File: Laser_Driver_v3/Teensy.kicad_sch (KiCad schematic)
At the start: 2 parts, among them U37 CR2013-MI2120

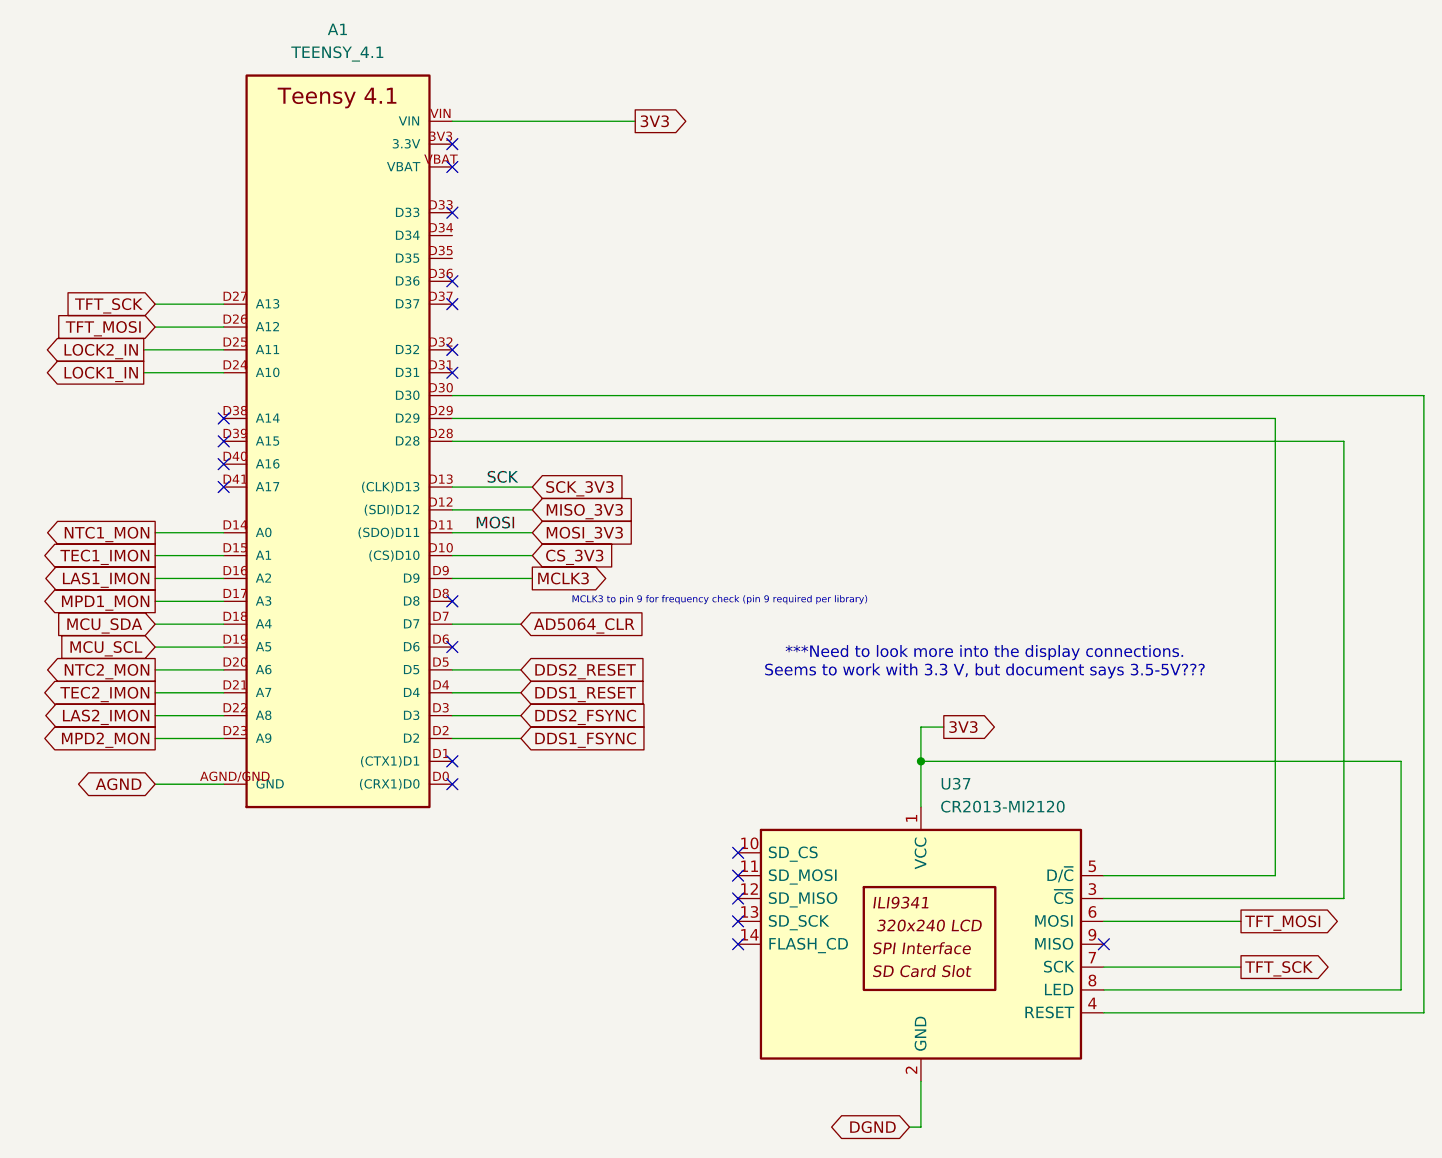
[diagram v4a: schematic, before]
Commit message: Many changes.  Working through ERC.
Main changes are for the grounds.  I found the NETTIE function to tie the GND, DGND and AGND together at a specific point on the boud with a footprint even.
Changed transformers one more time to be consistent for both.
Updated footprints to be consistent and avoid power input/output errors with the ERC.
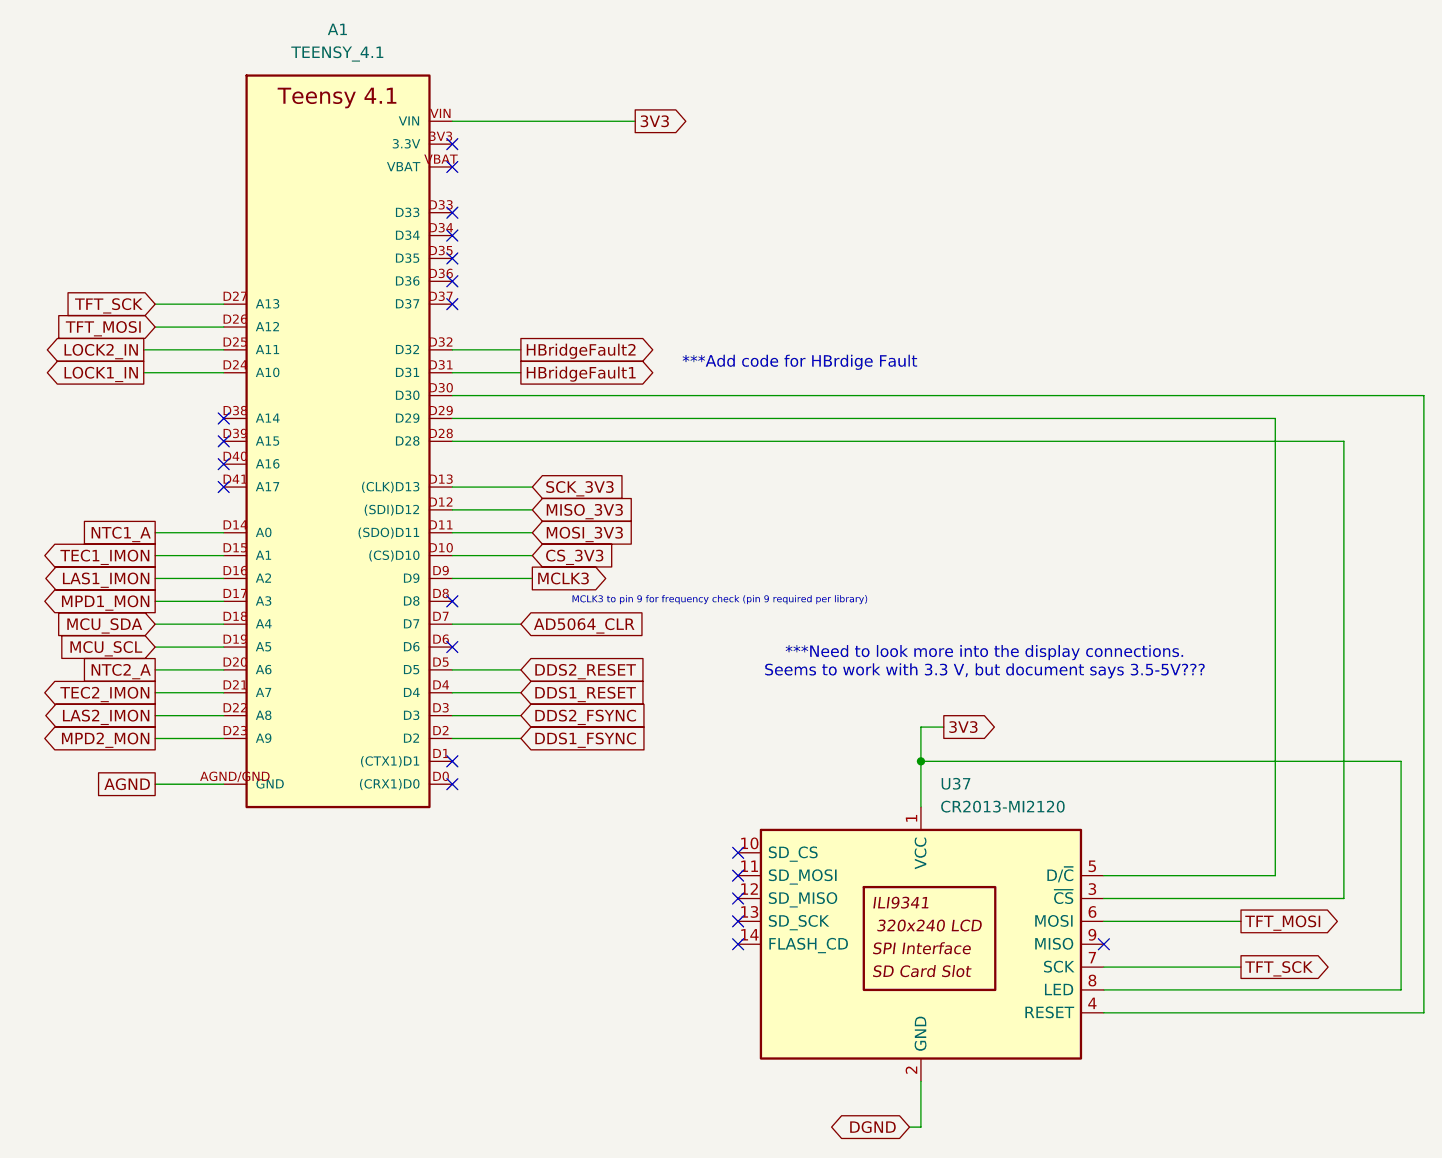
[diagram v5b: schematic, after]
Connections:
- net HBridgeFault1: now reaches A1.D31
- net HBridgeFault2: now reaches A1.D32
- net NTC1_MON renamed NTC1_A
- net NTC2_MON renamed NTC2_A
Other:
- note added: "***Add code for HBrdige Fault"
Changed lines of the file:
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@@
 	(generator_version "10.0")
 	(paper "A4")
+	(text "***Add code for HBrdige Fault"
+		(exclude_from_sim no)
+		(at 116.078 61.214 0)
+		(effects
+			(font
+				(size 1.27 1.27)
+			)
+		)
+	)
 	(text "***Need to look more into the display connections.\nSeems to work with 3.3 V, but document says 3.5-5V???\n"
 		(exclude_from_sim no)
@@
 	)
 	(no_connect
-		(at 77.47 62.23)
-	)
-	(no_connect
 		(at 77.47 92.71)
 	)
@@
 	)
 	(no_connect
-		(at 77.47 59.69)
-	)
-	(no_connect
 		(at 77.47 105.41)
 	)
@@
 	)
 	(no_connect
+		(at 77.47 46.99)
+	)
+	(no_connect
 		(at 149.86 125.73)
 	)
 	(no_connect
+		(at 77.47 49.53)
+	)
+	(no_connect
 		(at 52.07 74.93)
 	)
@@
 	(wire
 		(pts
+			(xy 77.47 62.23) (xy 85.09 62.23)
+		)
+		(stroke
+			(width 0)
+			(type default)
+		)
+	)
+	(wire
+		(pts
 			(xy 44.45 107.95) (xy 52.07 107.95)
 		)
@@
 	(wire
 		(pts
+			(xy 77.47 59.69) (xy 85.09 59.69)
+		)
+		(stroke
+			(width 0)
+			(type default)
+		)
+	)
+	(wire
+		(pts
 			(xy 77.47 97.79) (xy 85.09 97.79)
 		)
@@
 		)
 	)
-	(label "SCK"
-		(at 81.28 74.93 0)
-		(effects
-			(font
-				(size 1.27 1.27)
-			)
-			(justify left bottom)
-		)
-	)
-	(label "MOSI"
-		(at 80.01 80.01 0)
-		(effects
-			(font
-				(size 1.27 1.27)
-			)
-			(justify left bottom)
-		)
-	)
 	(global_label "CS_3V3"
 		(shape input)
@@
 		)
 	)
+	(global_label "HBridgeFault2"
+		(shape output)
+		(at 85.09 59.69 0)
+		(fields_autoplaced yes)
+		(effects
+			(font
+				(size 1.27 1.27)
+			)
+			(justify left)
+		)
+		(property "Intersheetrefs" "${INTERSHEET_REFS}"
+			(at 101.4403 59.69 0)
+			(hide yes)
+			(show_name no)
+			(do_not_autoplace no)
+			(effects
+				(font
+					(size 1.27 1.27)
+				)
+				(justify left)
+			)
+		)
+	)
 	(global_label "MOSI_3V3"
 		(shape input)
@@
 		)
 	)
+	(global_label "HBridgeFault1"
+		(shape output)
+		(at 85.09 62.23 0)
+		(fields_autoplaced yes)
+		(effects
+			(font
+				(size 1.27 1.27)
+			)
+			(justify left)
+		)
+		(property "Intersheetrefs" "${INTERSHEET_REFS}"
+			(at 101.4403 62.23 0)
+			(hide yes)
+			(show_name no)
+			(do_not_autoplace no)
+			(effects
+				(font
+					(size 1.27 1.27)
+				)
+				(justify left)
+			)
+		)
+	)
 	(global_label "TFT_MOSI"
 		(shape output)
@@
 		)
 	)
-	(global_label "NTC1_MON"
-		(shape output)
+	(global_label "NTC1_A"
+		(shape passive)
 		(at 44.45 80.01 180)
 		(fields_autoplaced yes)
@@
 		)
 		(property "Intersheetrefs" "${INTERSHEET_REFS}"
-			(at 31.6072 80.01 0)
+			(at 35.7423 80.01 0)
 			(hide yes)
 			(show_name no)
@@
 	)
 	(global_label "AGND"
-		(shape bidirectional)
+		(shape passive)
 		(at 44.45 107.95 180)
 		(fields_autoplaced yes)
@@
 		)
 		(property "Intersheetrefs" "${INTERSHEET_REFS}"
-			(at 35.3944 107.95 0)
+			(at 37.617 107.95 0)
 			(hide yes)
 			(show_name no)
@@
 		)
 	)
-	(global_label "NTC2_MON"
-		(shape output)
+	(global_label "NTC2_A"
+		(shape passive)
 		(at 44.45 95.25 180)
 		(fields_autoplaced yes)
@@
 		)
 		(property "Intersheetrefs" "${INTERSHEET_REFS}"
-			(at 31.6072 95.25 0)
+			(at 35.7423 95.25 0)
 			(hide yes)
 			(show_name no)

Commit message: Added software limit to TEC current, Hbridge Fault
Software limit to TEC current.  Monitors up to 2.5 A, then flags and reduces setting.
Hbridge fault now wired to Teensy and software flags.
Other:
- note removed: "***Add code for HBrdige Fault"
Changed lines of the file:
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@@
 	(generator_version "10.0")
 	(paper "A4")
-	(text "***Add code for HBrdige Fault"
-		(exclude_from_sim no)
-		(at 116.078 61.214 0)
-		(effects
-			(font
-				(size 1.27 1.27)
-			)
-		)
-	)
 	(text "***Need to look more into the display connections.\nSeems to work with 3.3 V, but document says 3.5-5V???\n"
 		(exclude_from_sim no)

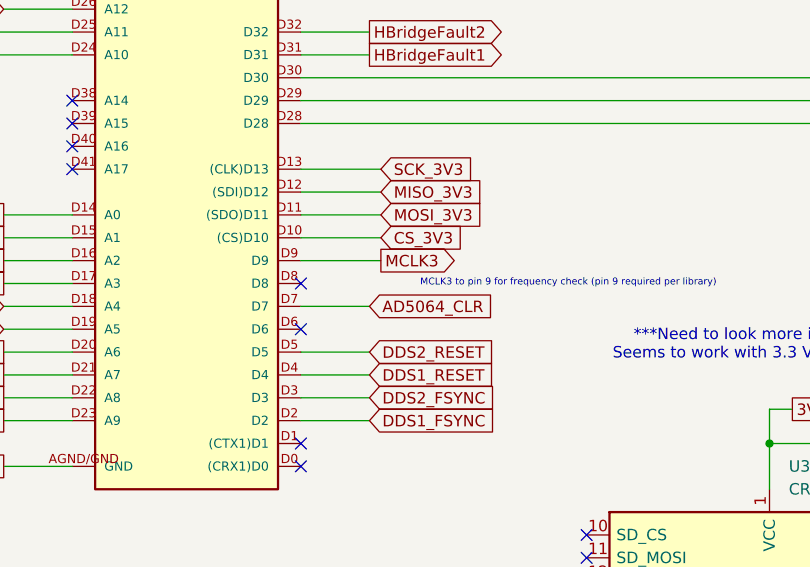
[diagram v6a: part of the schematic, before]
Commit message: 6 V supply. Annotations. Teensy zero current.
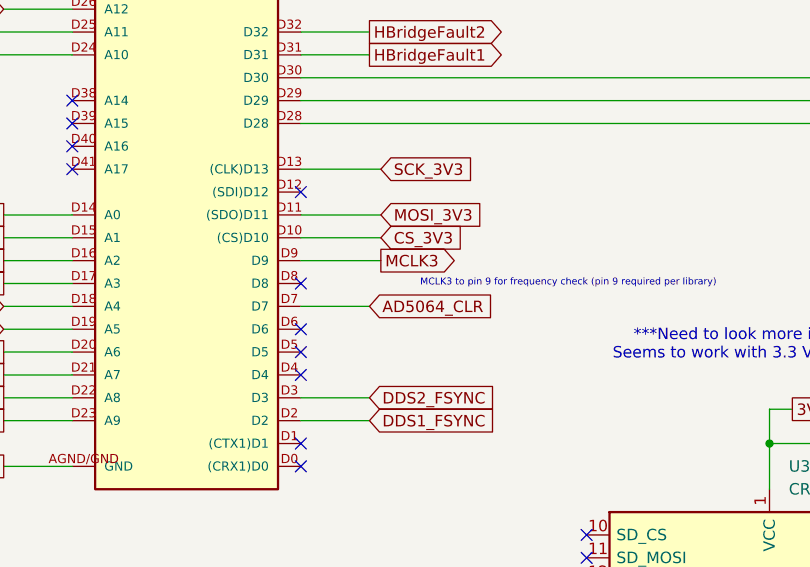
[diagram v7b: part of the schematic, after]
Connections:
- net DDS1_RESET: no longer names the net of A1.D4
- net DDS2_RESET: no longer names the net of A1.D5
- net MISO_3V3: no longer names the net of A1.D12 ((SDI)D12)
- no-connect marks 21 -> 24
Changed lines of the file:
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@@
 	)
 	(no_connect
+		(at 77.47 97.79)
+	)
+	(no_connect
+		(at 77.47 77.47)
+	)
+	(no_connect
 		(at 77.47 107.95)
 	)
@@
 	)
 	(no_connect
+		(at 77.47 95.25)
+	)
+	(no_connect
 		(at 109.22 118.11)
 	)
@@
 	(wire
 		(pts
-			(xy 77.47 77.47) (xy 86.36 77.47)
-		)
-		(stroke
-			(width 0)
-			(type default)
-		)
-	)
-	(wire
-		(pts
 			(xy 77.47 59.69) (xy 85.09 59.69)
 		)
@@
 	(wire
 		(pts
-			(xy 77.47 97.79) (xy 85.09 97.79)
-		)
-		(stroke
-			(width 0)
-			(type default)
-		)
-	)
-	(wire
-		(pts
 			(xy 77.47 102.87) (xy 85.09 102.87)
 		)
@@
 	(wire
 		(pts
-			(xy 77.47 95.25) (xy 85.09 95.25)
-		)
-		(stroke
-			(width 0)
-			(type default)
-		)
-	)
-	(wire
-		(pts
 			(xy 44.45 102.87) (xy 52.07 102.87)
 		)
@@
 		)
 	)
-	(global_label "DDS1_RESET"
-		(shape input)
-		(at 85.09 97.79 0)
-		(fields_autoplaced yes)
-		(effects
-			(font
-				(size 1.27 1.27)
-			)
-			(justify left)
-		)
-		(property "Intersheetrefs" "${INTERSHEET_REFS}"
-			(at 99.7469 97.79 0)
-			(hide yes)
-			(show_name no)
-			(do_not_autoplace no)
-			(effects
-				(font
-					(size 1.27 1.27)
-				)
-				(justify left)
-			)
-		)
-	)
 	(global_label "MPD1_MON"
 		(shape output)
@@
 		)
 	)
-	(global_label "DDS2_RESET"
-		(shape input)
-		(at 85.09 95.25 0)
-		(fields_autoplaced yes)
-		(effects
-			(font
-				(size 1.27 1.27)
-			)
-			(justify left)
-		)
-		(property "Intersheetrefs" "${INTERSHEET_REFS}"
-			(at 99.7469 95.25 0)
-			(hide yes)
-			(show_name no)
-			(do_not_autoplace no)
-			(effects
-				(font
-					(size 1.27 1.27)
-				)
-				(justify left)
-			)
-		)
-	)
 	(global_label "HBridgeFault2"
 		(shape output)
@@
 			(hide yes)
 			(show_name no)
-			(do_not_autoplace no)
-			(effects
-				(font
-					(size 1.27 1.27)
-				)
-				(justify left)
-			)
-		)
-	)
-	(global_label "MISO_3V3"
-		(shape input)
-		(at 86.36 77.47 0)
-		(fields_autoplaced yes)
-		(effects
-			(font
-				(size 1.27 1.27)
-			)
-			(justify left)
-		)
-		(property "Intersheetrefs" "${INTERSHEET_REFS}"
-			(at 98.4166 77.47 0)
-			(hide yes)
-			(show_name no)
